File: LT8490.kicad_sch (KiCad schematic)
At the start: 118 parts, among them J1 Conn_01x01, J10 Conn_01x01, J11 Conn_01x01, J12 Conn_01x01, J13 Conn_01x01, J14 Conn_01x01, J15 Conn_01x01, J16 Conn_01x01, J17 Conn_01x01, J18 Conn_01x01, J19 Conn_01x01, J2 Conn_01x01, J20 Conn_01x01, J21 Conn_01x01, J22 Conn_01x01, J23 Conn_01x01, J24 Conn_01x01, J25 Conn_01x01, J3 Conn_01x01, J4 Conn_01x01, J5 Conn_01x01, J6 Conn_01x01, J7 Conn_01x01, J8 Conn_01x01, J9 Conn_01x01, Q1 Si7106DN, Q2 Si7106DN, Q3 Si7106DN, Q4 Si7106DN, Q5 BSS84, Q6 MBT2222ADW1T1, U4 LT8490EUKJPBF

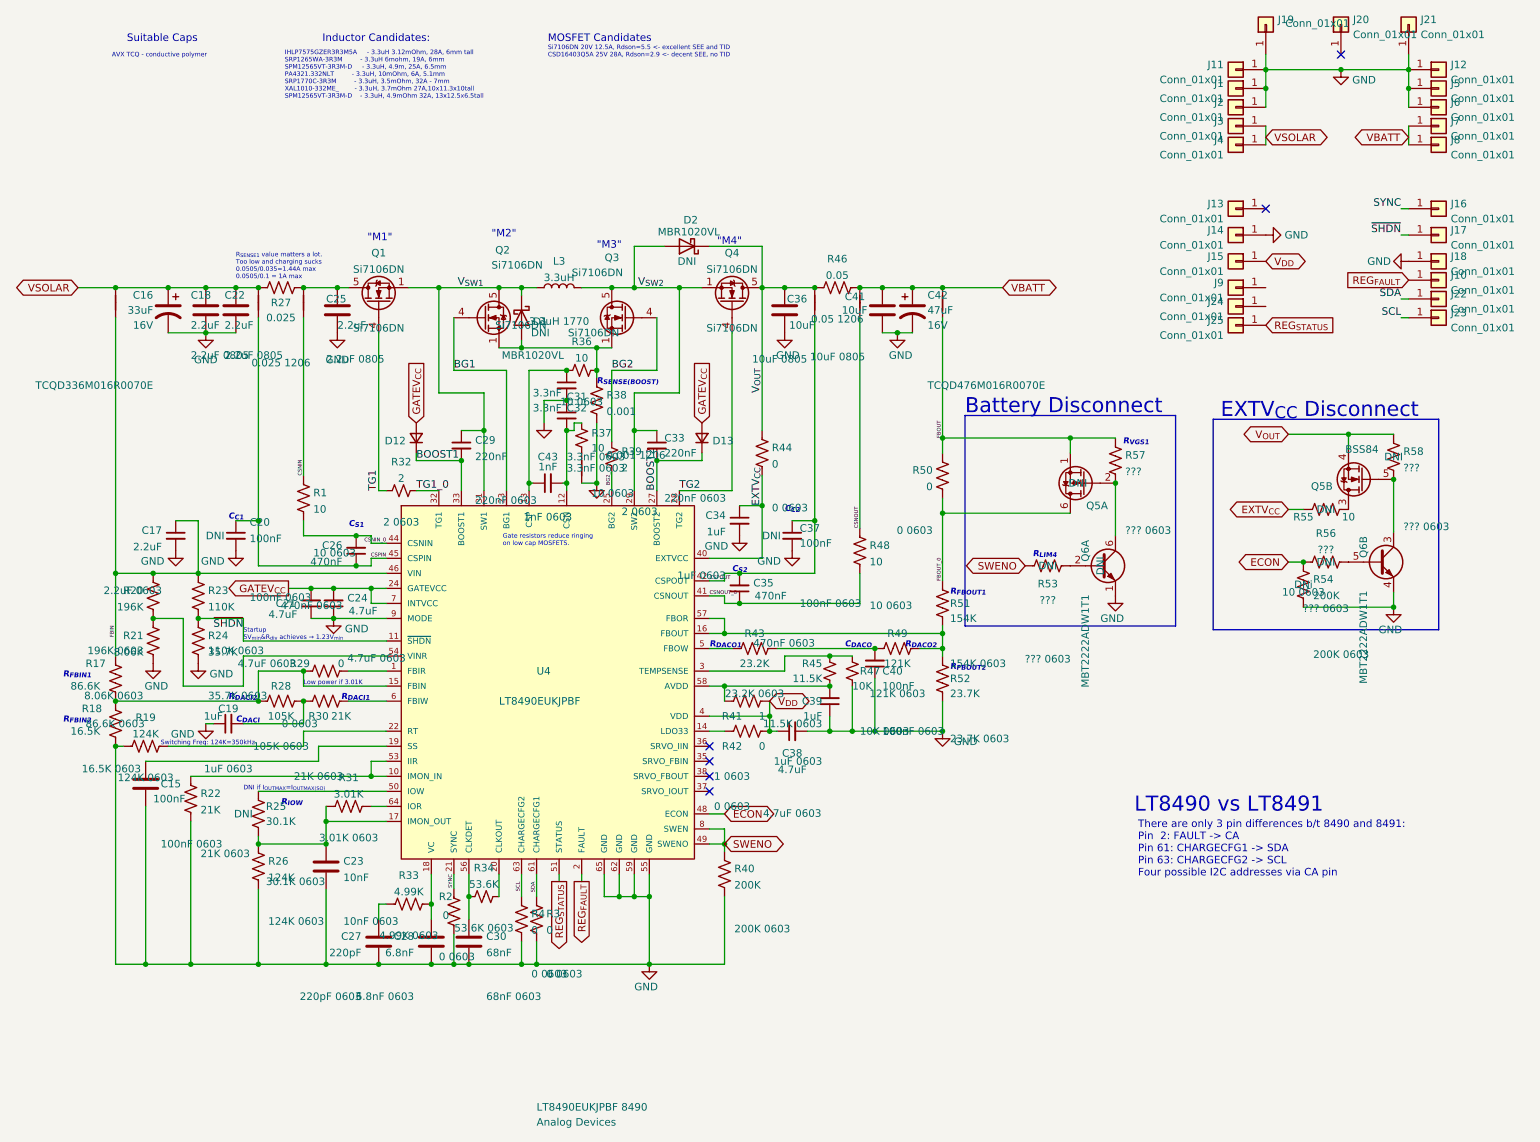
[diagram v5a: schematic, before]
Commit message: Added module highlights and part justifications to readme
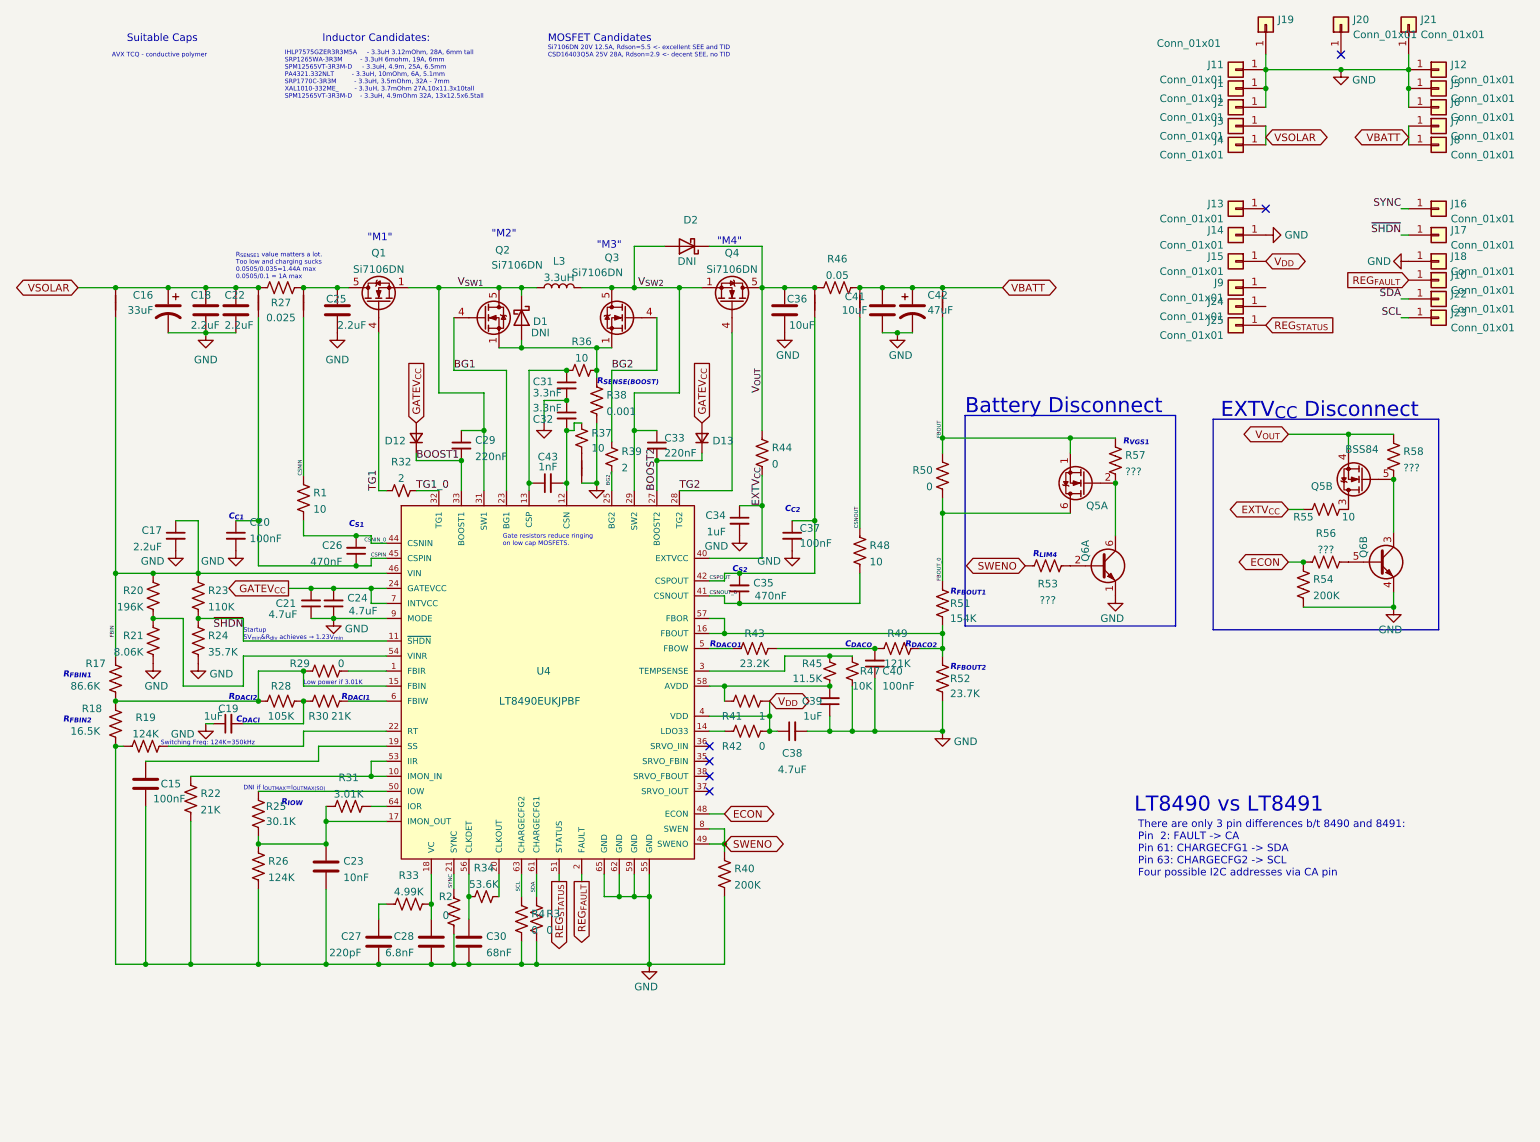
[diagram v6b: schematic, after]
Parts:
- D1, D2: value MBR1020VL -> (none); footprint Diode_SMD:D_SOD-123F -> (none)
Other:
- note added: "IHLP7575GZER3R3M5A - 3.3uH 3.12mOhm, 28A, 6mm tall SRP1265WA-3R3M - 3.3uH 6mohm, 19A, 6mm SPM12565VT-3R3M-D - 3.3uH, 4.9m, 25A, 6.5mm PA4321.332NLT - 3.3uH, 10mOhm, 6A, 5.1mm SRP1770C-3R3M - 3.3uH, 3.5mOhm, 32A - 7mm XAL1010-332ME_ - 3.3uH, 3.7mOhm 27A,10x11.3x10tall SPM12565VT-3R3M-D - 3.3uH, 4.9mOhm 32A, 13x12.5x6.5tall"
- note removed: "IHLP7575GZER3R3M5A t- 3.3uH 3.12mOhm, 28A, 6mm tall SRP1265WA-3R3M tt- 3.3uH 6mohm, 19A, 6mm SPM12565VT-3R3M-D t- 3.3uH, 4.9m, 25A, 6.5mm PA4321.332NLT tt- 3.3uH, 10mOhm, 6A, 5.1mm SRP1770C-3R3M tt- 3.3uH, 3.5mOhm, 32A - 7mm XAL1010-332ME_tt- 3.3uH, 3.7mOhm 27A,10x11.3x10tall SPM12565VT-3R3M-Dt- 3.3uH, 4.9mOhm 32A, 13x12.5x6.5tall"

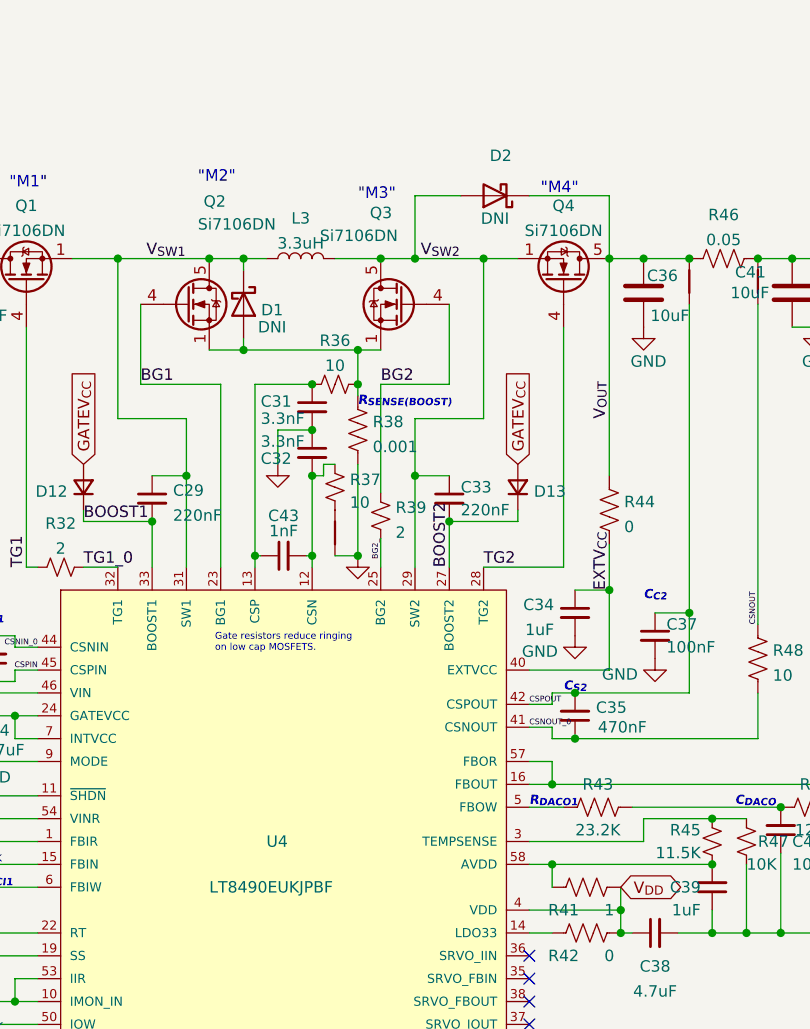
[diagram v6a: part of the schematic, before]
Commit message: plane cleanup
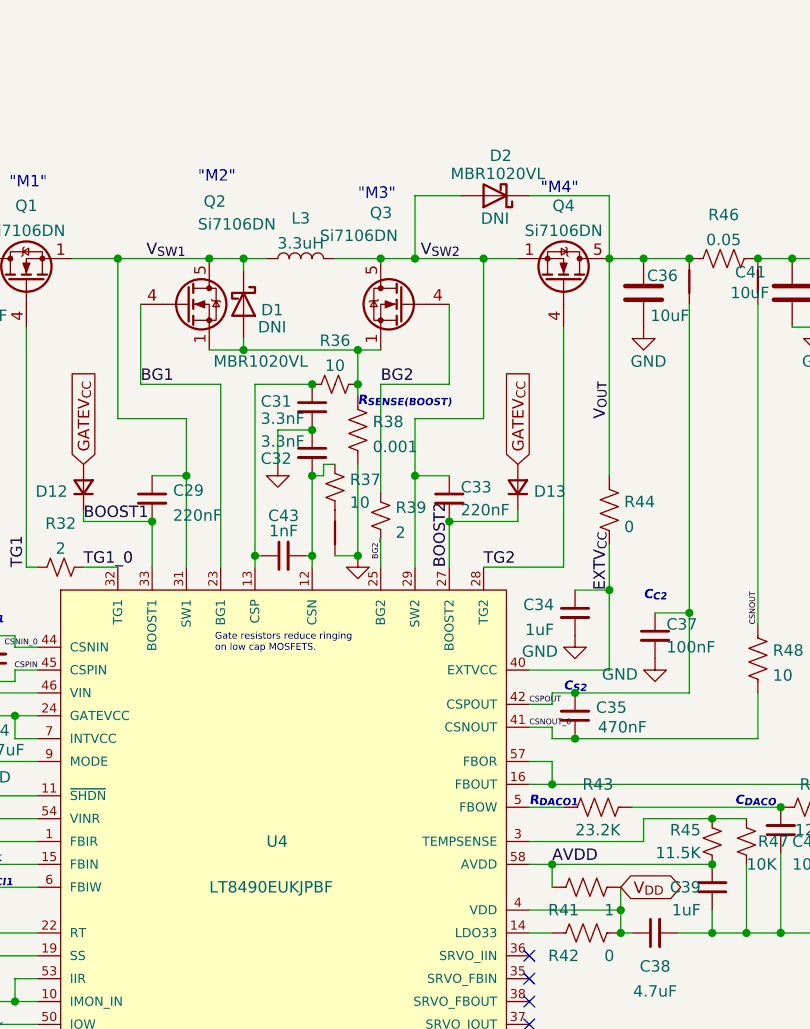
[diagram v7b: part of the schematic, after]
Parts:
- D1, D2: value (none) -> MBR1020VL; footprint (none) -> Diode_SMD:D_SOD-123F
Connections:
- net AVDD: now reaches C39.2, R41.2, R45.2, U4.58 (AVDD)
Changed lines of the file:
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@@
+    (effects (font (size 1.27 1.27)) (justify left bottom))
+  )
+  (label "AVDD" (at 147.32 128.27 0)
     (effects (font (size 1.27 1.27)) (justify left bottom))
   )
@@
     (in_bom yes) (on_board yes)
     (property "Reference" "D2" (id 0) (at 141.605 49.53 0))
-    (property "Value" "" (id 1) (at 141.2875 51.5421 0))
-    (property "Footprint" "" (id 2) (at 140.97 53.975 0)
+    (property "Value" "MBR1020VL" (id 1) (at 141.2875 51.5421 0))
+    (property "Footprint" "Diode_SMD:D_SOD-123F" (id 2) (at 140.97 53.975 0)
       (effects (font (size 1.27 1.27)) hide)
     )
@@
     (in_bom yes) (on_board yes)
     (property "Reference" "D1" (id 0) (at 116.205 66.675 90))
-    (property "Value" "" (id 1) (at 114.935 72.39 90))
-    (property "Footprint" "" (id 2) (at 113.03 66.04 0)
-      (effects (font (size 1.27 1.27)) hide)
-    )
+    (property "Value" "MBR1020VL" (id 1) (at 114.935 72.39 90))
+    (property "Footprint" "Diode_SMD:D_SOD-123F" (id 2) (at 113.03 66.04 0)
+      (effects (font (size 1.27 1.27)) hide)
+    )

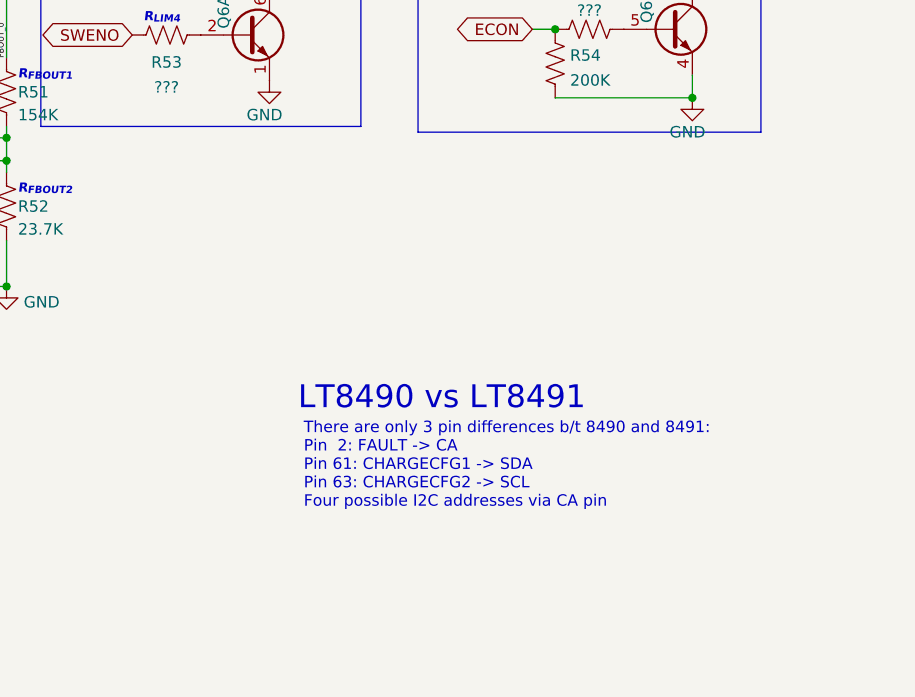
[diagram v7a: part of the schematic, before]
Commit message: added i2c address resistors to CA
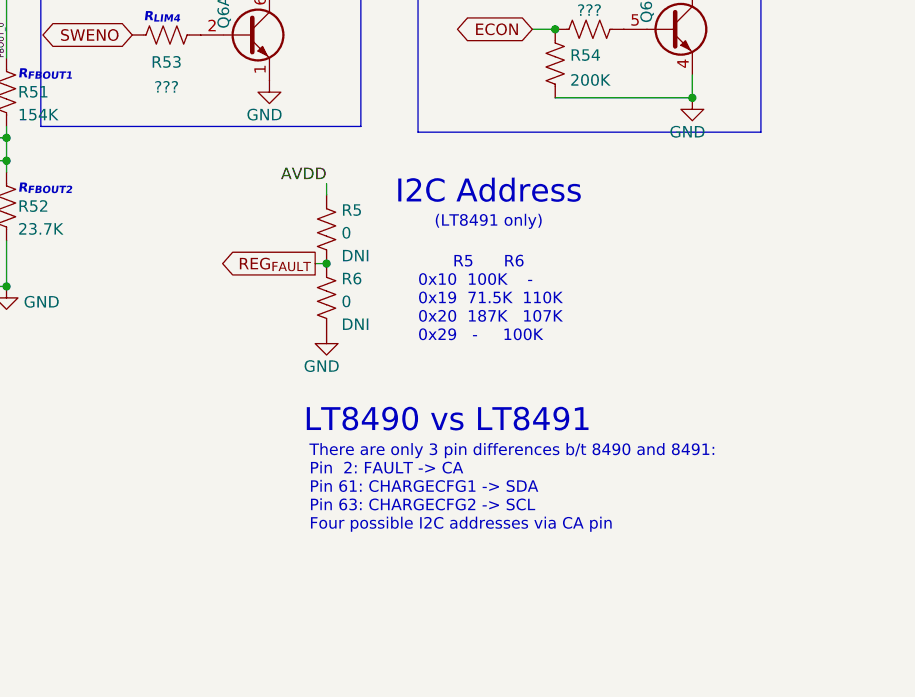
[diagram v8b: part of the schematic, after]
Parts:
- added R5, R6: 0, Resistor_SMD:R_0402_1005Metric, symbol Device:R_US
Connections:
- net AVDD: now also R5.1
- net GND: now also R6.2
- net REG_{FAULT}: now also R5.2, R6.1
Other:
- note added: "(LT8491 only)"
- note added: "I2C Address"
- note added: "R5 R6 0x10 100K - 0x19 71.5K 110K 0x20 187K 107K 0x29 - 100K"
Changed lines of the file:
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@@
   (junction (at 262.89 27.305) (diameter 0) (color 0 0 0 0)
   )
+  (junction (at 219.71 133.35) (diameter 0) (color 0 0 0 0)
+  )
   (junction (at 260.35 93.345) (diameter 0) (color 0 0 0 0)
   )
@@
     (stroke (width 0) (type default) (color 0 0 0 0))
   )
+  (wire (pts (xy 219.71 124.46) (xy 219.71 125.73))
+    (stroke (width 0) (type default) (color 0 0 0 0))
+  )
   (wire (pts (xy 125.73 71.12) (xy 128.27 71.12))
     (stroke (width 0) (type default) (color 0 0 0 0))
@@
     (stroke (width 0) (type default) (color 0 0 0 0))
   )
+  (wire (pts (xy 218.44 133.35) (xy 219.71 133.35))
+    (stroke (width 0) (type default) (color 0 0 0 0))
+  )
   (wire (pts (xy 99.06 60.96) (xy 109.22 60.96))
     (stroke (width 0) (type default) (color 0 0 0 0))
@@
   )
   (text "There are only 3 pin differences b/t 8490 and 8491:\nPin  2: FAULT -> CA\nPin 61: CHARGECFG1 -> SDA\nPin 63: CHARGECFG2 -> SCL\nFour possible I2C addresses via CA pin"
-    (at 217.17 160.655 0)
+    (at 217.805 163.195 0)
     (effects (font (size 1.27 1.27)) (justify left bottom))
   )
@@
     (effects (font (size 1.016 1.016) (thickness 0.254) bold italic) (justify left bottom))
   )
+  (text "	   R5	  R6\n0x10  100K    -\n0x19  71.5K  110K\n0x20  187K   107K\n0x29   -     100K"
+    (at 229.87 142.24 0)
+    (effects (font (size 1.27 1.27)) (justify left bottom))
+  )
   (text "IHLP7575GZER3R3M5A 	- 3.3uH 3.12mOhm, 28A, 6mm tall\nSRP1265WA-3R3M 		- 3.3uH 6mohm, 19A, 6mm \nSPM12565VT-3R3M-D 	- 3.3uH, 4.9m, 25A, 6.5mm \nPA4321.332NLT 		- 3.3uH, 10mOhm, 6A, 5.1mm\nSRP1770C-3R3M 		- 3.3uH, 3.5mOhm, 32A - 7mm\nXAL1010-332ME_		- 3.3uH, 3.7mOhm 27A,10x11.3x10tall\nSPM12565VT-3R3M-D	- 3.3uH, 4.9mOhm 32A, 13x12.5x6.5tall"
     (at 73.025 29.21 0)
@@
     (effects (font (size 1.016 1.016) (thickness 0.254) bold italic) (justify left bottom))
   )
+  (text " (LT8491 only)" (at 231.14 129.54 0)
+    (effects (font (size 1.27 1.27)) (justify left bottom))
+  )
   (text "MOSFET Candidates" (at 117.475 19.685 0)
     (effects (font (size 1.27 1.27)) (justify left bottom))
@@
     (effects (font (size 1.016 1.016) (thickness 0.254) bold italic) (justify left bottom))
   )
-  (text "LT8490 vs LT8491" (at 216.535 149.86 0)
+  (text "LT8490 vs LT8491" (at 217.17 152.4 0)
     (effects (font (size 2.54 2.54)) (justify left bottom))
   )
@@
     (effects (font (size 1.016 1.016) (thickness 0.254) bold italic) (justify left bottom))
   )
+  (text "I2C Address" (at 227.33 127 0)
+    (effects (font (size 2.54 2.54)) (justify left bottom))
+  )
   (label "TG1" (at 88.9 95.25 90)
     (effects (font (size 1.27 1.27)) (justify left bottom))
@@
     (effects (font (size 1.27 1.27)) (justify left bottom))
   )
+  (label "AVDD" (at 219.71 124.46 180)
+    (effects (font (size 1.27 1.27)) (justify right bottom))
+  )
   (label "SCL" (at 113.03 161.29 270)
     (effects (font (size 0.635 0.635)) (justify right bottom))
@@
     )
   )
+  (global_label "REG_{FAULT}" (shape output) (at 218.44 133.35 180) (fields_autoplaced)
+    (effects (font (size 1.27 1.27)) (justify right))
+    (property "Intersheet References" "${INTERSHEET_REFS}" (id 0) (at 208.0241 133.2706 0)
+      (effects (font (size 1.27 1.27)) (justify right) hide)
+    )
+  )
   (symbol (lib_id "Device:NetTie_2") (at 68.58 63.5 90) (unit 1)
     (in_bom yes) (on_board yes) (fields_autoplaced)
@@
     (pin "2")
   )
+  (symbol (lib_id "power:GND") (at 219.71 140.97 0) (unit 1)
+    (in_bom yes) (on_board yes)
+    (property "Reference" "#PWR?" (id 0) (at 219.71 147.32 0)
+      (effects (font (size 1.27 1.27)) hide)
+    )
+    (property "Value" "GND" (id 1) (at 217.17 144.78 0)
+      (effects (font (size 1.27 1.27)) (justify left))
+    )
+    (property "Footprint" "" (id 2) (at 219.71 140.97 0)
+      (effects (font (size 1.27 1.27)) hide)
+    )
+    (property "Datasheet" "" (id 3) (at 219.71 140.97 0)
+      (effects (font (size 1.27 1.27)) hide)
+    )
+    (pin "1")
+  )
   (symbol (lib_id "Device:R_Small_US") (at 92.71 95.25 270) (unit 1)
     (in_bom yes) (on_board yes) (fields_autoplaced)
@@
     (pin "2")
   )
+  (symbol (lib_id "Device:R_US") (at 219.71 137.16 0) (unit 1)
+    (in_bom yes) (on_board yes) (fields_autoplaced)
+    (property "Reference" "R6" (id 0) (at 221.361 135.0569 0)
+      (effects (font (size 1.27 1.27)) (justify left))
+    )
+    (property "Value" "0" (id 1) (at 221.361 137.5938 0)
+      (effects (font (size 1.27 1.27)) (justify left))
+    )
+    (property "Footprint" "Resistor_SMD:R_0402_1005Metric" (id 2) (at 220.726 137.414 90)
+      (effects (font (size 1.27 1.27)) hide)
+    )
+    (property "Datasheet" "~" (id 3) (at 219.71 137.16 0)
+      (effects (font (size 1.27 1.27)) hide)
+    )
+    (property "Description" "10 0603" (id 4) (at 221.361 146.4115 0)
+      (effects (font (size 1.27 1.27)) (justify left) hide)
+    )
+    (property "DNI" "DNI" (id 5) (at 221.361 140.1307 0)
+      (effects (font (size 1.27 1.27)) (justify left))
+    )
+    (pin "1")
+    (pin "2")
+  )
   (symbol (lib_id "power:GND") (at 262.89 56.515 270) (unit 1)
     (in_bom yes) (on_board yes)
@@
     (pin "1")
   )
+  (symbol (lib_id "Device:R_US") (at 219.71 129.54 0) (unit 1)
+    (in_bom yes) (on_board yes) (fields_autoplaced)
+    (property "Reference" "R5" (id 0) (at 221.361 127.4369 0)
+      (effects (font (size 1.27 1.27)) (justify left))
+    )
+    (property "Value" "0" (id 1) (at 221.361 129.9738 0)
+      (effects (font (size 1.27 1.27)) (justify left))
+    )
+    (property "Footprint" "Resistor_SMD:R_0402_1005Metric" (id 2) (at 220.726 129.794 90)
+      (effects (font (size 1.27 1.27)) hide)
+    )
+    (property "Datasheet" "~" (id 3) (at 219.71 129.54 0)
+      (effects (font (size 1.27 1.27)) hide)
+    )
+    (property "Description" "10 0603" (id 4) (at 221.361 138.7915 0)
+      (effects (font (size 1.27 1.27)) (justify left) hide)
+    )
+    (property "DNI" "DNI" (id 5) (at 221.361 132.5107 0)
+      (effects (font (size 1.27 1.27)) (justify left))
+    )
+    (pin "1")
+    (pin "2")
+  )
   (symbol (lib_id "Transistor_FET:Si7336ADP") (at 88.9 63.5 90) (unit 1)
     (in_bom yes) (on_board yes) (fields_autoplaced)
@@
       (reference "#PWR0128") (unit 1) (value "GND") (footprint "")
     )
+    (path "/7373b6a4-abf0-408b-bb8f-eef8e15a1fa6"
+      (reference "#PWR?") (unit 1) (value "GND") (footprint "")
+    )
     (path "/acb1e74d-a19c-4f23-b04a-efc44089f9fa"
       (reference "C15") (unit 1) (value "100nF") (footprint "Capacitor_SMD:C_0603_1608Metric")
@@
       (reference "R4") (unit 1) (value "0") (footprint "Resistor_SMD:R_0603_1608Metric")
     )
+    (path "/f8350471-e61b-4db2-997c-0ddc5e67581f"
+      (reference "R5") (unit 1) (value "0") (footprint "Resistor_SMD:R_0402_1005Metric")
+    )
+    (path "/990ababb-3d01-42e7-bd8d-8da143da99ce"
+      (reference "R6") (unit 1) (value "0") (footprint "Resistor_SMD:R_0402_1005Metric")
+    )
     (path "/8c9b241c-1d18-4f70-8eb0-c75268d36f6f"
